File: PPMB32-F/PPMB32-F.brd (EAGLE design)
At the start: 78.7 x 69.5 mm, 35 parts, among them IC1 7805TV, Q1 SS8050-G, Q2 SS8050-G, SW1 P-B1720, U1 AMS1117-3.3, U2 ESP32-WROOM-32D, U3 CP2102N-A01-GQFN28

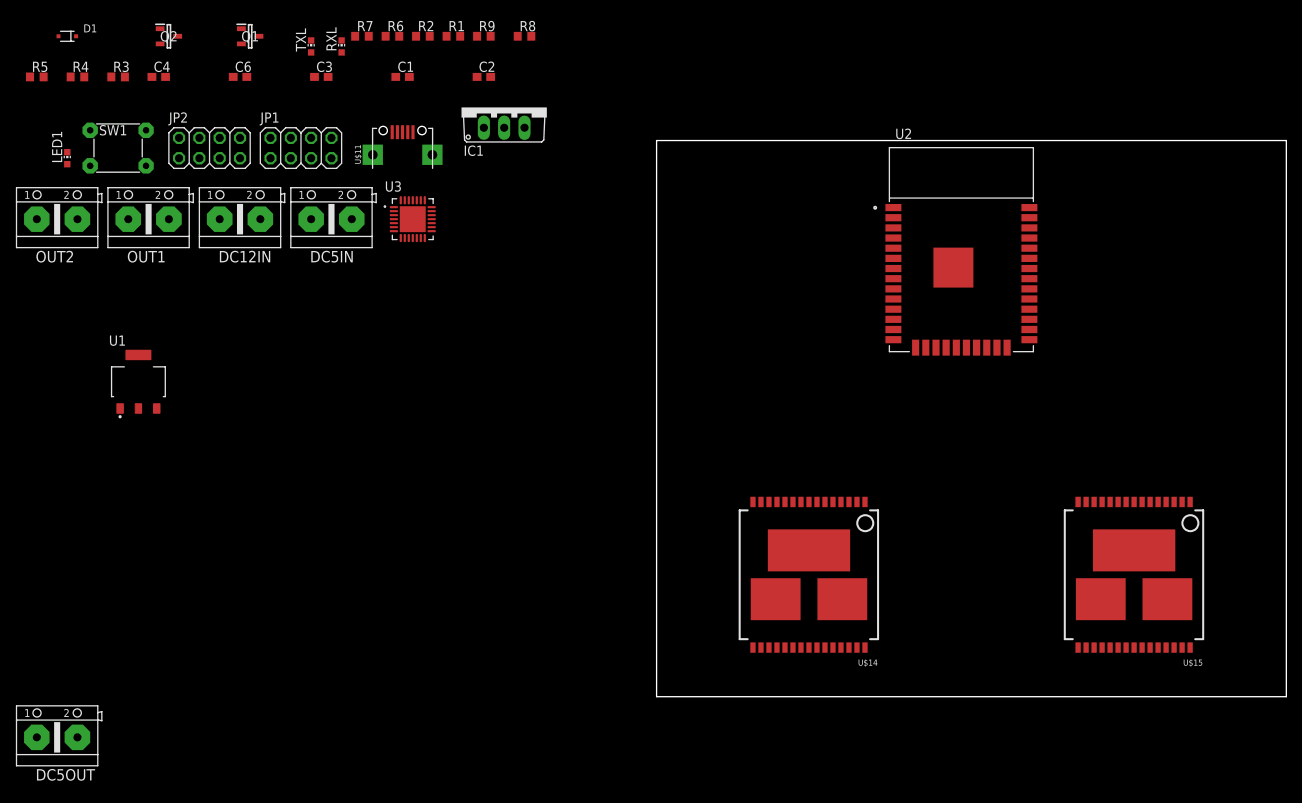
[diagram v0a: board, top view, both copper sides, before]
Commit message: Edit PPMB32-E; prepare PPSB-T for sending gerbers to JLCPCB
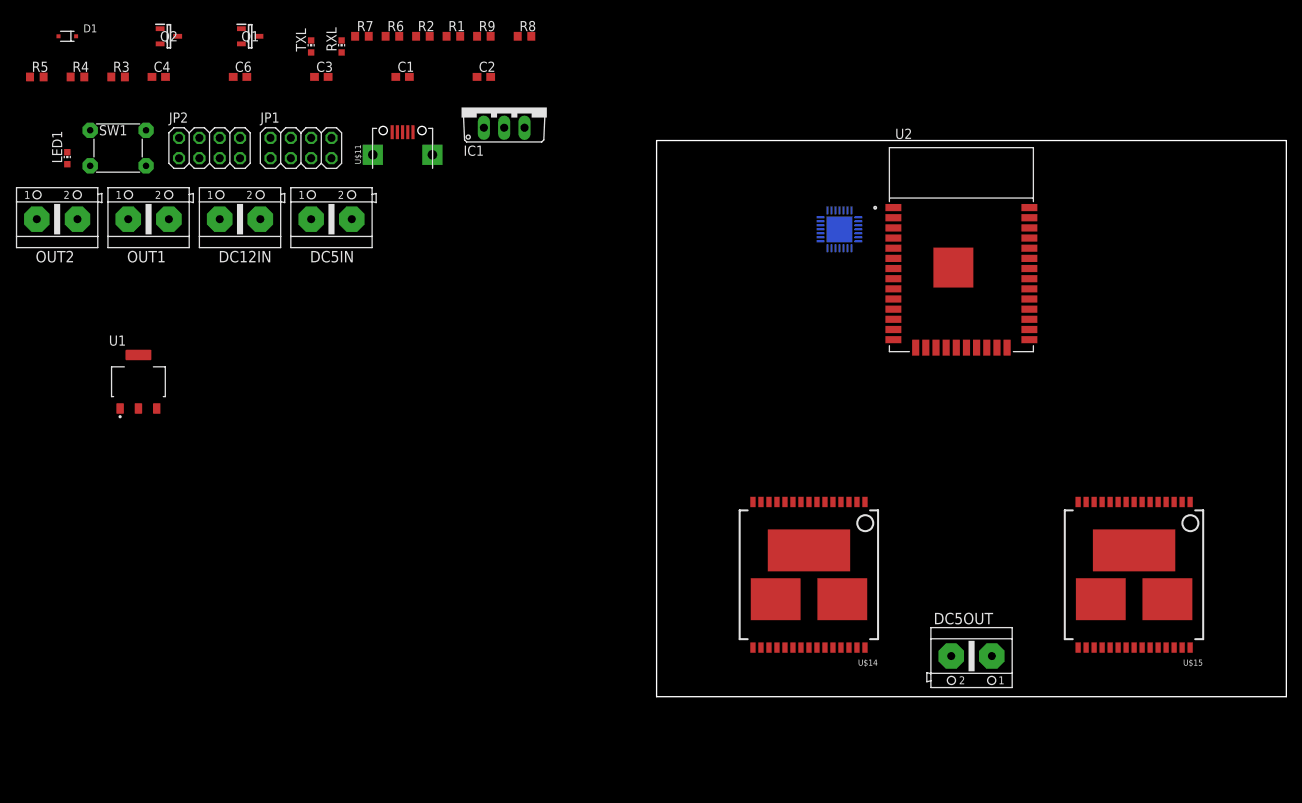
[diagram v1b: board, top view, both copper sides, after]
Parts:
- moved DC5OUT 114.8 mm to (39.4, 5.08), turned to 180 degrees
- moved U3 53.4 mm to (22.9, 58.4), flipped to the bottom
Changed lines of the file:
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@@
 <attribute name="VALUE" x="29.133040625" y="40.2645" size="1.2738" layer="27"/>
 </element>
-<element name="U3" library="CP2102N-A01-GQFN28" package="QFN50P500X500X80-29N" value="CP2102N-A01-GQFN28" x="-30.48" y="59.69" smashed="yes">
-<attribute name="AVAILABILITY" value="Unavailable" x="0" y="0" size="1.778" layer="27" display="off"/>
-<attribute name="DESCRIPTION" value=" USB Bridge, USB to UART USB 2.0 UART Interface 28-QFN _5x5_ " x="0" y="0" size="1.778" layer="27" display="off"/>
-<attribute name="MF" value="Silicon Labs" x="0" y="0" size="1.778" layer="27" display="off"/>
-<attribute name="MP" value="CP2102N-A01-GQFN28" x="0" y="0" size="1.778" layer="27" display="off"/>
-<attribute name="NAME" x="-33.9802" y="63.140109375" size="1.27245" layer="25"/>
-<attribute name="PACKAGE" value="QFN-28 Silicon Labs" x="0" y="0" size="1.778" layer="27" display="off"/>
-<attribute name="PRICE" value="None" x="0" y="0" size="1.778" layer="27" display="off"/>
-<attribute name="VALUE" x="-33.83426875" y="55.009290625" size="1.272540625" layer="27"/>
-</element>
-<element name="DC5OUT" library="#PaJa_konektory" package="ARK500/2" value="+5VOUT" x="-74.93" y="-5.08" smashed="yes">
-<attribute name="NAME" x="-77.625" y="-10.478" size="1.4224" layer="25"/>
-<attribute name="VALUE" x="-79.6393" y="-8.41" size="1.016" layer="27"/>
+<element name="U3" library="CP2102N-A01-GQFN28" package="QFN50P500X500X80-29N" value="CP2102N-A01-GQFN28" x="22.86" y="58.42" smashed="yes" rot="MR0">
+<attribute name="AVAILABILITY" value="Unavailable" x="-7.62" y="-1.27" size="1.778" layer="28" rot="MR0" display="off"/>
+<attribute name="DESCRIPTION" value=" USB Bridge, USB to UART USB 2.0 UART Interface 28-QFN _5x5_ " x="-7.62" y="-1.27" size="1.778" layer="28" rot="MR0" display="off"/>
+<attribute name="MF" value="Silicon Labs" x="-7.62" y="-1.27" size="1.778" layer="28" rot="MR0" display="off"/>
+<attribute name="MP" value="CP2102N-A01-GQFN28" x="-7.62" y="-1.27" size="1.778" layer="28" rot="MR0" display="off"/>
+<attribute name="NAME" x="26.3602" y="61.870109375" size="1.27245" layer="26" rot="MR0"/>
+<attribute name="PACKAGE" value="QFN-28 Silicon Labs" x="-7.62" y="-1.27" size="1.778" layer="28" rot="MR0" display="off"/>
+<attribute name="PRICE" value="None" x="-7.62" y="-1.27" size="1.778" layer="28" rot="MR0" display="off"/>
+<attribute name="VALUE" x="26.21426875" y="53.739290625" size="1.272540625" layer="28" rot="MR0"/>
+</element>
+<element name="DC5OUT" library="#PaJa_konektory" package="ARK500/2" value="+5VOUT" x="39.37" y="5.08" smashed="yes" rot="R180">
+<attribute name="NAME" x="42.065" y="10.478" size="1.4224" layer="25" rot="R180"/>
+<attribute name="VALUE" x="44.0793" y="8.41" size="1.016" layer="27" rot="R180"/>
 </element>
 <element name="U$14" library="SparkFun-IC-Special-Function" package="VNH2SP30" value="VNH2SP30" x="19.05" y="15.24" smashed="yes" rot="R180">
@@
 <contactref element="JP1" pad="8"/>
 <contactref element="DC5OUT" pad="2"/>
-<wire x1="-67.06" y1="36.025" x2="-72.39" y2="-5.08" width="0" layer="19" extent="1-1"/>
+<wire x1="-67.06" y1="36.025" x2="36.83" y2="5.08" width="0" layer="19" extent="1-1"/>
 <wire x1="-73.66" y1="68.06" x2="-67.06" y2="36.025" width="0" layer="19" extent="1-1"/>
 <wire x1="-70.8025" y1="70.8025" x2="-73.66" y2="68.06" width="0" layer="19" extent="1-1"/>
@@
 <wire x1="-41.06" y1="77.47" x2="-39.37" y2="80.53" width="0" layer="19" extent="1-1"/>
 <wire x1="-43.18" y1="80.53" x2="-41.06" y2="77.47" width="0" layer="19" extent="1-1"/>
-<wire x1="-32.84" y1="60.19" x2="-35.475" y2="67.74" width="0" layer="19" extent="1-1"/>
-<wire x1="-30.48" y1="59.69" x2="-32.84" y2="60.19" width="0" layer="19" extent="1-1"/>
-<wire x1="-38.1" y1="59.69" x2="-32.84" y2="60.19" width="0" layer="19" extent="1-1"/>
+<wire x1="25.22" y1="58.92" x2="-35.475" y2="67.74" width="0" layer="19" extent="1-1"/>
+<wire x1="22.86" y1="58.42" x2="25.22" y2="58.92" width="0" layer="19" extent="1-1"/>
+<wire x1="-38.1" y1="59.69" x2="25.22" y2="58.92" width="0" layer="19" extent="1-1"/>
 <wire x1="-19.05" y1="71.12" x2="-28.025" y2="67.74" width="0" layer="19" extent="1-1"/>
 <wire x1="-22.44" y1="77.47" x2="-19.05" y2="71.12" width="0" layer="19" extent="1-1"/>
-<wire x1="29.6" y1="61.14" x2="-30.48" y2="59.69" width="0" layer="19" extent="1-1"/>
+<wire x1="29.6" y1="61.14" x2="22.86" y2="58.42" width="0" layer="19" extent="1-1"/>
 <wire x1="37.1" y1="53.64" x2="29.6" y2="61.14" width="0" layer="19" extent="1-1"/>
 <wire x1="32.385" y1="43.63" x2="37.1" y2="53.64" width="0" layer="19" extent="1-1"/>
@@
 <wire x1="-30.9" y1="77.47" x2="-20.74" y2="77.47" width="0" layer="19" extent="1-1"/>
 <wire x1="-30.06" y1="82.55" x2="-30.9" y2="77.47" width="0" layer="19" extent="1-1"/>
-<wire x1="-32.84" y1="58.69" x2="-30.9" y2="77.47" width="0" layer="19" extent="1-1"/>
-<wire x1="-32.84" y1="58.19" x2="-32.84" y2="58.69" width="0" layer="19" extent="1-1"/>
-<wire x1="29.6" y1="59.87" x2="-32.84" y2="58.19" width="0" layer="19" extent="1-1"/>
+<wire x1="25.22" y1="57.42" x2="-30.9" y2="77.47" width="0" layer="19" extent="1-1"/>
+<wire x1="25.22" y1="56.92" x2="25.22" y2="57.42" width="0" layer="19" extent="1-1"/>
+<wire x1="29.6" y1="59.87" x2="25.22" y2="56.92" width="0" layer="19" extent="1-1"/>
 <wire x1="-64.77" y1="36.025" x2="29.6" y2="59.87" width="0" layer="19" extent="1-1"/>
 </signal>
@@
 <contactref element="R8" pad="1"/>
 <contactref element="Q2" pad="2"/>
-<wire x1="-31.98" y1="62.05" x2="-17.36" y2="82.55" width="0" layer="19" extent="1-1"/>
-<wire x1="-62.06" y1="81.6" x2="-31.98" y2="62.05" width="0" layer="19" extent="1-1"/>
+<wire x1="24.36" y1="60.78" x2="-17.36" y2="82.55" width="0" layer="19" extent="1-1"/>
+<wire x1="-62.06" y1="81.6" x2="24.36" y2="60.78" width="0" layer="19" extent="1-1"/>
 </signal>
 <signal name="USB_DN">
 <contactref element="U3" pad="5"/>
 <contactref element="U$11" pad="2"/>
-<wire x1="-32.84" y1="59.19" x2="-32.4" y2="70.565" width="0" layer="19" extent="1-1"/>
+<wire x1="25.22" y1="57.92" x2="-32.4" y2="70.565" width="0" layer="19" extent="1-1"/>
 </signal>
 <signal name="USB_DP">
 <contactref element="U3" pad="4"/>
 <contactref element="U$11" pad="3"/>
-<wire x1="-32.84" y1="59.69" x2="-31.75" y2="70.565" width="0" layer="19" extent="1-1"/>
+<wire x1="25.22" y1="58.42" x2="-31.75" y2="70.565" width="0" layer="19" extent="1-1"/>
 </signal>
 <signal name="N$1">
 <contactref element="U3" pad="9"/>
 <contactref element="R2" pad="2"/>
-<wire x1="-31.48" y1="57.33" x2="-28.36" y2="82.55" width="0" layer="19" extent="1-1"/>
+<wire x1="23.86" y1="56.06" x2="-28.36" y2="82.55" width="0" layer="19" extent="1-1"/>
 </signal>
 <signal name="N$9">
 <contactref element="R3" pad="1"/>
 <contactref element="U3" pad="12"/>
-<wire x1="-68.16" y1="77.47" x2="-29.98" y2="57.33" width="0" layer="19" extent="1-1"/>
+<wire x1="-68.16" y1="77.47" x2="22.36" y2="56.06" width="0" layer="19" extent="1-1"/>
 </signal>
 <signal name="N$10">
@@
 <contactref element="R4" pad="1"/>
 <contactref element="R5" pad="1"/>
-<wire x1="-73.24" y1="77.47" x2="-31.98" y2="57.33" width="0" layer="19" extent="1-1"/>
+<wire x1="-73.24" y1="77.47" x2="24.36" y2="56.06" width="0" layer="19" extent="1-1"/>
 <wire x1="-78.32" y1="77.47" x2="-73.24" y2="77.47" width="0" layer="19" extent="1-1"/>
 </signal>
@@
 <contactref element="U3" pad="25"/>
 <contactref element="R6" pad="2"/>
-<wire x1="-30.48" y1="62.05" x2="-32.17" y2="82.55" width="0" layer="19" extent="1-1"/>
+<wire x1="22.86" y1="60.78" x2="-32.17" y2="82.55" width="0" layer="19" extent="1-1"/>
 </signal>
 <signal name="TXD">
 <contactref element="U3" pad="26"/>
 <contactref element="R7" pad="2"/>
-<wire x1="-30.98" y1="62.05" x2="-35.98" y2="82.55" width="0" layer="19" extent="1-1"/>
+<wire x1="23.36" y1="60.78" x2="-35.98" y2="82.55" width="0" layer="19" extent="1-1"/>
 </signal>
 <signal name="RTS">
@@
 <contactref element="R9" pad="1"/>
 <contactref element="Q1" pad="2"/>
-<wire x1="-29.98" y1="62.05" x2="-22.44" y2="82.55" width="0" layer="19" extent="1-1"/>
-<wire x1="-51.9" y1="81.6" x2="-29.98" y2="62.05" width="0" layer="19" extent="1-1"/>
+<wire x1="22.36" y1="60.78" x2="-22.44" y2="82.55" width="0" layer="19" extent="1-1"/>
+<wire x1="-51.9" y1="81.6" x2="22.36" y2="60.78" width="0" layer="19" extent="1-1"/>
 </signal>
 <signal name="CTS">
@@
 <contactref element="JP1" pad="1"/>
 <contactref element="DC5OUT" pad="1"/>
-<wire x1="-48.26" y1="67.31" x2="-77.47" y2="-5.08" width="0" layer="19" extent="1-1"/>
+<wire x1="-48.26" y1="67.31" x2="41.91" y2="5.08" width="0" layer="19" extent="1-1"/>
 <wire x1="-45.72" y1="67.31" x2="-48.26" y2="67.31" width="0" layer="19" extent="1-1"/>
 <wire x1="-43.18" y1="67.31" x2="-45.72" y2="67.31" width="0" layer="19" extent="1-1"/>
